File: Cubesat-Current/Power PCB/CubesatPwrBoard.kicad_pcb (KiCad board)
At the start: 2 copper layers, 90 x 96 mm, 57 parts, among them J1 SystemLoad, J10 Test_Point, J11 Test_Point, J14 Test_Point, J15 Test_Point, J16 Test_Point_GND, J2 SystemLoad, J3 I2C, J6 Test_Point, J7 Test_Point, Q1 TQM110NB04CR_RLG, Q2 2N7002*, U1 LTC4162

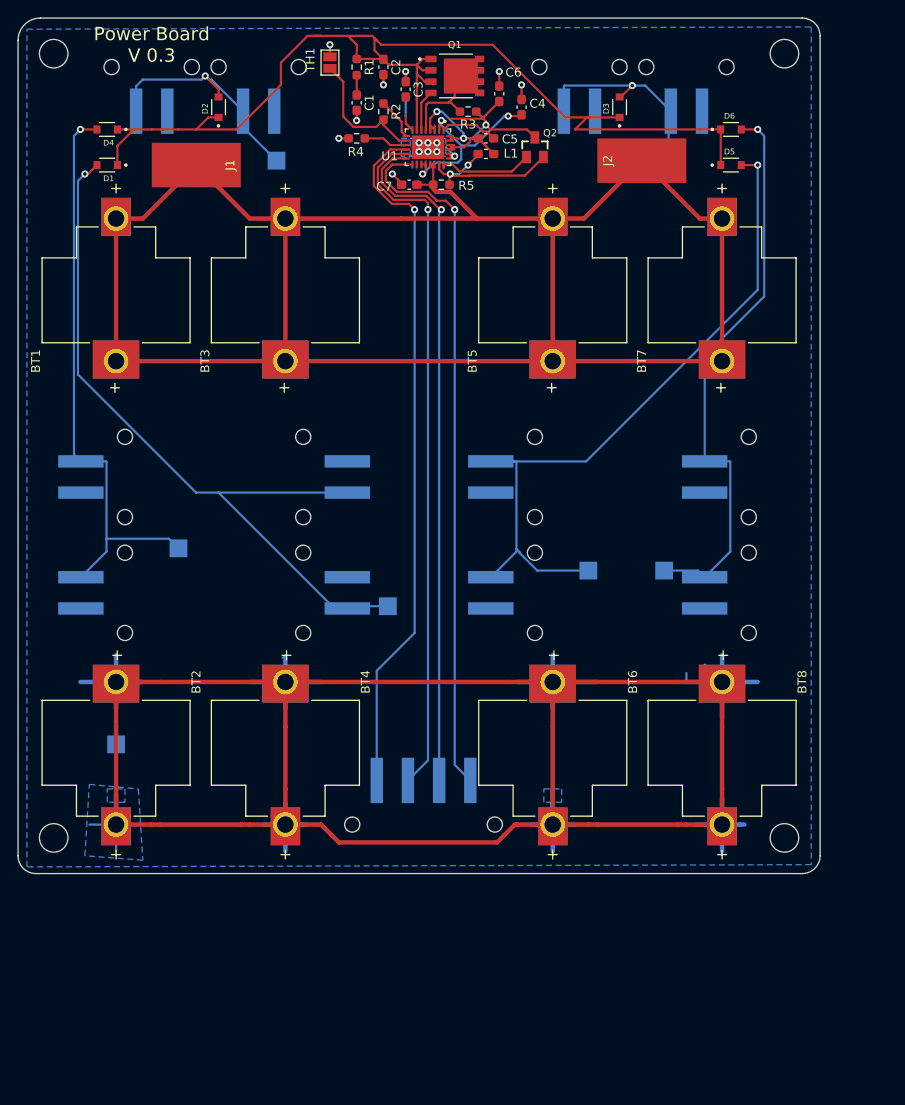
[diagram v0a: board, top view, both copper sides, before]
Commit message: Major revision to power board, three battery design v1
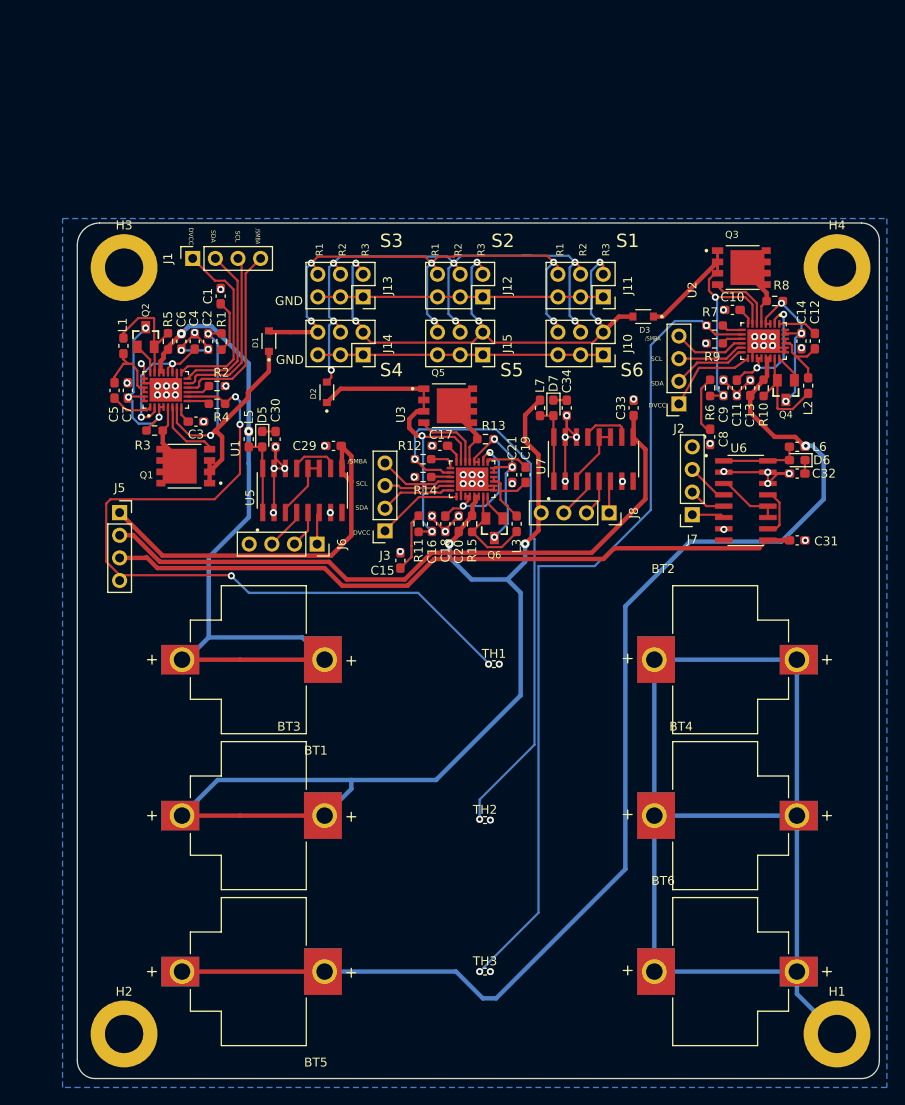
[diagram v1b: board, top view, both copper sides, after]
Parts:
- removed BT7, BT8: 254TR, 254TR:BAT_254TR
- removed D4: D_Schottky_Small, CUS520,H3F:DIO_CUS520,H3F
- removed J16: Test_Point_GND, TestPoint:TestPoint_Pad_2.0x2.0mm
- removed REF** (x4): MountingHole_3.2mm_M3, MountingHole:MountingHole_3.2mm_M3
- removed SC1, SC10, SC11, SC12, SC2, SC3, SC4, SC5, SC6, SC7, SC8, SC9: Solar_Cells, 6915_1x2:691508110302
- added C10: 1u, Capacitor_SMD:C_0603_1608Metric_Pad1.08x0.95mm_HandSolder, F.Cu at (180.2, 55.2)
- added C11: 4.7u, Capacitor_SMD:C_0603_1608Metric_Pad1.08x0.95mm_HandSolder, F.Cu at (180.7, 64.0)
- added C12: C, Capacitor_SMD:C_0603_1608Metric_Pad1.08x0.95mm_HandSolder, F.Cu at (189.4, 58.8)
- added C13: 10u, Capacitor_SMD:C_0603_1608Metric_Pad1.08x0.95mm_HandSolder, F.Cu at (182.2, 64.0)
- added C14: 10u, Capacitor_SMD:C_0603_1608Metric_Pad1.08x0.95mm_HandSolder, F.Cu at (187.9, 58.8)
- added C15: 150u, Capacitor_SMD:C_0603_1608Metric_Pad1.08x0.95mm_HandSolder, F.Cu at (142.9, 83.4)
- added C16: C_Polarized_US, Capacitor_SMD:C_0603_1608Metric_Pad1.08x0.95mm_HandSolder, F.Cu at (146.5, 79.2)
- added C17: 1u, Capacitor_SMD:C_0603_1608Metric_Pad1.08x0.95mm_HandSolder, F.Cu at (147.3, 70.5)
- added C18: 4.7u, Capacitor_SMD:C_0603_1608Metric_Pad1.08x0.95mm_HandSolder, F.Cu at (148.0, 79.2)
- added C19: C, Capacitor_SMD:C_0603_1608Metric_Pad1.08x0.95mm_HandSolder, F.Cu at (157.0, 73.8)
- added C20: 10u, Capacitor_SMD:C_0603_1608Metric_Pad1.08x0.95mm_HandSolder, F.Cu at (149.5, 79.2)
- added C21: 10u, Capacitor_SMD:C_0603_1608Metric_Pad1.08x0.95mm_HandSolder, F.Cu at (155.5, 73.8)
- added C29: C_Polarized_US, Capacitor_SMD:C_0603_1608Metric_Pad1.08x0.95mm_HandSolder, F.Cu at (135.4, 70.5)
- added C30: C_Polarized_US, Capacitor_SMD:C_0603_1608Metric_Pad1.08x0.95mm_HandSolder, F.Cu at (128.9, 69.8)
- added C31: 4.7u, Capacitor_SMD:C_0603_1608Metric_Pad1.08x0.95mm_HandSolder, F.Cu at (187.4, 81.1)
- added C32: 100u, Capacitor_SMD:C_0603_1608Metric_Pad1.08x0.95mm_HandSolder, F.Cu at (187.4, 73.6)
- added C33: 4.7u, Capacitor_SMD:C_0603_1608Metric_Pad1.08x0.95mm_HandSolder, F.Cu at (169.1, 66.2)
- added C34: 100u, Capacitor_SMD:C_0603_1608Metric_Pad1.08x0.95mm_HandSolder, F.Cu at (161.6, 66.2)
- added C8: 150u, Capacitor_SMD:C_0603_1608Metric_Pad1.08x0.95mm_HandSolder, F.Cu at (177.7, 69.5)
- added C9: C_Polarized_US, Capacitor_SMD:C_0603_1608Metric_Pad1.08x0.95mm_HandSolder, F.Cu at (179.2, 64.0)
- added D7: D_Schottky, Diode_SMD:D_0603_1608Metric_Pad1.05x0.95mm_HandSolder, F.Cu at (160.1, 66.2)
- added H1: MountingHole_Pad, MountingHole:MountingHole_4.3mm_M4_DIN965_Pad, F.Cu at (191.9, 136.5)
- added H2: MountingHole_Pad, MountingHole:MountingHole_4.3mm_M4_DIN965_Pad, F.Cu at (111.9, 136.5)
- added H3: MountingHole_Pad, MountingHole:MountingHole_4.3mm_M4_DIN965_Pad, F.Cu at (111.9, 50.5)
- added H4: MountingHole_Pad, MountingHole:MountingHole_4.3mm_M4_DIN965_Pad, F.Cu at (191.9, 50.5)
- added J12: S3, Connector_PinSocket_2.54mm:PinSocket_2x03_P2.54mm_Vertical, F.Cu at (152.2, 53.8)
- added J13: S4, Connector_PinSocket_2.54mm:PinSocket_2x03_P2.54mm_Vertical, F.Cu at (138.7, 53.8)
- added J5: Conn_01x04_Female, Connector_PinSocket_2.54mm:PinSocket_1x04_P2.54mm_Vertical, F.Cu at (111.4, 78.0)
- added J8: Conn_01x03_Female, Connector_PinSocket_2.54mm:PinSocket_1x04_P2.54mm_Vertical, F.Cu at (166.3, 78.0)
- added L2: 4.7u, Inductor_SMD:L_0603_1608Metric_Pad1.05x0.95mm_HandSolder, F.Cu at (188.7, 63.8)
- added L3: 4.7u, Inductor_SMD:L_0603_1608Metric_Pad1.05x0.95mm_HandSolder, F.Cu at (156.0, 79.2)
- added L5: L, Inductor_SMD:L_0603_1608Metric_Pad1.05x0.95mm_HandSolder, F.Cu at (125.9, 69.8)
- added L6: 22u, Inductor_SMD:L_0603_1608Metric_Pad1.05x0.95mm_HandSolder, F.Cu at (187.4, 70.6)
- added L7: 22u, Inductor_SMD:L_0603_1608Metric_Pad1.05x0.95mm_HandSolder, F.Cu at (158.6, 66.2)
- added Q3: TQM110NB04CR_RLG, TQM110N:TRANS_TQM110NB04CR_RLG, F.Cu at (181.2, 50.5)
- added Q4: 2N7002*, 2N7002:SOT23, F.Cu at (186.2, 64.2)
- added Q5: TQM110NB04CR_RLG, TQM110N:TRANS_TQM110NB04CR_RLG, F.Cu at (148.2, 66.0)
- added Q6: 2N7002*, 2N7002:SOT23, F.Cu at (153.5, 79.8)
- added R10: 10m, Resistor_SMD:R_0603_1608Metric_Pad0.98x0.95mm_HandSolder, F.Cu at (183.7, 64.0)
- added R11: 2.5, Resistor_SMD:R_0603_1608Metric_Pad0.98x0.95mm_HandSolder, F.Cu at (145.0, 79.2)
- added R12: 16m, Resistor_SMD:R_0603_1608Metric_Pad0.98x0.95mm_HandSolder, F.Cu at (145.5, 72.0)
- added R13: 16m, Resistor_SMD:R_0603_1608Metric_Pad0.98x0.95mm_HandSolder, F.Cu at (152.5, 69.8)
- added R14: 63.4k, Resistor_SMD:R_0603_1608Metric_Pad0.98x0.95mm_HandSolder, F.Cu at (145.5, 74.0)
- added R15: 10m, Resistor_SMD:R_0603_1608Metric_Pad0.98x0.95mm_HandSolder, F.Cu at (151.0, 79.2)
- added R6: 2.5, Resistor_SMD:R_0603_1608Metric_Pad0.98x0.95mm_HandSolder, F.Cu at (177.7, 64.0)
- added R7: 16m, Resistor_SMD:R_0603_1608Metric_Pad0.98x0.95mm_HandSolder, F.Cu at (178.2, 57.0)
- added R8: 16m, Resistor_SMD:R_0603_1608Metric_Pad0.98x0.95mm_HandSolder, F.Cu at (184.9, 54.2)
- added R9: 63.4k, Resistor_SMD:R_0603_1608Metric_Pad0.98x0.95mm_HandSolder, F.Cu at (178.2, 59.0)
- added TH2: Thermistor_NTC, Resistor_SMD:R_0402_1005Metric_Pad0.72x0.64mm_HandSolder, F.Cu at (152.4, 112.5)
- added TH3: Thermistor_NTC, Resistor_SMD:R_0402_1005Metric_Pad0.72x0.64mm_HandSolder, F.Cu at (152.4, 129.5)
- added U2: LTC4162, LTC4162:QFN50P500X400X80-29N, F.Cu at (183.7, 58.8)
- added U3: LTC4162, LTC4162:QFN50P500X400X80-29N, F.Cu at (151.0, 74.2)
- added U5: MAX710ESE+T, MAX710ESE:SOIC127P600X175-16N, F.Cu at (131.9, 75.5)
- added U6: MAX710ESE+T, MAX710ESE:SOIC127P600X175-16N, F.Cu at (181.7, 76.6)
- added U7: MAX710ESE+T, MAX710ESE:SOIC127P600X175-16N, F.Cu at (164.6, 72.0)
- C1: value 150u -> C_Polarized_US
- C2: value 0.1u -> C_Polarized_US
- C3: value 1u -> C
- C4: value 4.7u -> C
- C5: value 22n -> C
- C6, C7: value 10u -> C
- D5, D6: value D_Schottky_Small -> D_Schottky; footprint CUS520,H3F:DIO_CUS520,H3F -> Diode_SMD:D_0603_1608Metric_Pad1.05x0.95mm_HandSolder
- J1, J2: value SystemLoad -> Conn_01x04_Female; footprint Connector_Wire:SolderWirePad_1x01_SMD_5x10mm -> Connector_PinSocket_2.54mm:PinSocket_1x04_P2.54mm_Vertical
- J10: value Test_Point -> S1; footprint TestPoint:TestPoint_Pad_2.0x2.0mm -> Connector_PinSocket_2.54mm:PinSocket_2x03_P2.54mm_Vertical; moved to F.Cu
- J11: value Test_Point -> S2; footprint TestPoint:TestPoint_Pad_2.0x2.0mm -> Connector_PinSocket_2.54mm:PinSocket_2x03_P2.54mm_Vertical; moved to F.Cu
- J14: value Test_Point -> S5; footprint TestPoint:TestPoint_Pad_2.0x2.0mm -> Connector_PinSocket_2.54mm:PinSocket_2x03_P2.54mm_Vertical; moved to F.Cu
- J15: value Test_Point -> S6; footprint TestPoint:TestPoint_Pad_2.0x2.0mm -> Connector_PinSocket_2.54mm:PinSocket_2x03_P2.54mm_Vertical; moved to F.Cu
- J3: value I2C -> Conn_01x04_Female; footprint 6915_1x4:691508110304 -> Connector_PinSocket_2.54mm:PinSocket_1x04_P2.54mm_Vertical; moved to F.Cu
- J6, J7: value Test_Point -> Conn_01x03_Female; footprint TestPoint:TestPoint_Pad_2.0x2.0mm -> Connector_PinSocket_2.54mm:PinSocket_1x04_P2.54mm_Vertical; moved to F.Cu
- L1: value 4.7u -> L
- R1: value 2.5 -> R
- R2, R3: value 16m -> R
- R4: value 63.4k -> R
- R5: value 10m -> R
- TH1: footprint Jumper:SolderJumper-2_P1.3mm_Open_Pad1.0x1.5mm -> Resistor_SMD:R_0402_1005Metric_Pad0.72x0.64mm_HandSolder
- moved BT5 83.6 mm to (126.4, 129.5), turned to 180 degrees
- moved TH1 70.0 mm to (153.4, 95.0), turned to 0 degrees
- moved BT2 69.2 mm to (179.4, 94.5), turned to 0 degrees
- moved J7 61.3 mm to (175.7, 78.2), turned to 180 degrees
- moved D5 60.9 mm to (127.4, 69.8), turned to -90 degrees
- moved BT3 59.1 mm to (126.4, 112.0), turned to 180 degrees
- moved J11 55.4 mm to (165.7, 53.8), turned to -90 degrees
- moved Q1 53.2 mm to (118.8, 72.8), turned to 180 degrees
- moved C5 50.4 mm to (110.8, 64.3), turned to 90 degrees
- moved R3 50.2 mm to (115.3, 68.8), turned to 0 degrees
- moved BT4 49.9 mm to (179.4, 112.0), turned to 0 degrees
- moved Q2 48.6 mm to (114.3, 58.3)
- moved L1 46.0 mm to (111.8, 59.3), turned to 90 degrees
- moved C6 45.2 mm to (118.3, 58.8), turned to -90 degrees
- moved C4 45.1 mm to (119.8, 58.8)
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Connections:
- net Net-(R2-Pad2) renamed /Bat_Reg_1/TH
- BT1 pad P1_1: Net-(BT1-PadP1_1) -> /Bat_Reg_1/V_Bat
- BT1 pad P1_2: Net-(BT1-PadP1_1) -> /Bat_Reg_1/V_Bat
- BT3 pad P1_1: Net-(BT1-PadP1_1) -> /Bat_Reg_2/V_Bat
- BT3 pad P1_2: Net-(BT1-PadP1_1) -> /Bat_Reg_2/V_Bat
- BT5 pad P1_1: Net-(BT1-PadP1_1) -> /Bat_Reg_3/V_Bat
- BT5 pad P1_2: Net-(BT1-PadP1_1) -> /Bat_Reg_3/V_Bat
- C2 pad 1: Net-(C2-Pad1) -> /Bat_Reg_1/VIN
- C6 pad 1: Net-(C6-Pad1) -> /Bat_Reg_1/V_Bat
- C7 pad 1: Net-(BT1-PadP1_1) -> Net-(C7-Pad1)
- D1 pad 1: Net-(C2-Pad1) -> /Bat_Reg_1/VIN
- D2 pad 1: Net-(C2-Pad1) -> /Bat_Reg_2/VIN
- D3 pad 1: Net-(C2-Pad1) -> /Bat_Reg_3/VIN
- D5 pad 1: Net-(C2-Pad1) -> Net-(C30-Pad1)
- D6 pad 1: Net-(C2-Pad1) -> Net-(C32-Pad1)
- J1 pad 1: Net-(BT1-PadP1_1) -> /Bat_Reg_1/DVCC
- J10 pad 1: Net-(D3-Pad2) -> GND
- J11 pad 1: Net-(D4-Pad2) -> GND
- J14 pad 1: Net-(D5-Pad2) -> GND
- J15 pad 1: Net-(D6-Pad2) -> GND
- J2 pad 1: Net-(BT1-PadP1_1) -> /Bat_Reg_3/DVCC
- J3 pad 1: Net-(J3-Pad1) -> /Bat_Reg_2/DVCC
- J3 pad 2: Net-(J3-Pad2) -> /Bat_Reg_2/SDA
- J3 pad 3: Net-(J3-Pad3) -> /Bat_Reg_2/SCL
- J3 pad 4: Net-(J3-Pad4) -> /Bat_Reg_2//SMBALERT
- J6 pad 1: Net-(D1-Pad2) -> /V_Reg_3.3_5V1/3/#5
- J7 pad 1: Net-(D2-Pad2) -> /V_Reg_3.3_5V3/3/#5
- Q1 pad 1: Net-(C2-Pad1) -> /Bat_Reg_1/VIN
- Q1 pad 2: Net-(C2-Pad1) -> /Bat_Reg_1/VIN
- Q1 pad 3: Net-(C2-Pad1) -> /Bat_Reg_1/VIN
- Q2 pad 3: Net-(C6-Pad1) -> Net-(C7-Pad1)
- R1 pad 1: Net-(C2-Pad1) -> /Bat_Reg_1/VIN
- R3 pad 1: Net-(C6-Pad1) -> Net-(C7-Pad1)
- R5 pad 1: Net-(BT1-PadP1_1) -> /Bat_Reg_1/V_Bat
- U1 pad 12: Net-(J3-Pad4) -> /Bat_Reg_1//SMBALERT
- U1 pad 13: Net-(J3-Pad3) -> /Bat_Reg_1/SCL
- U1 pad 14: Net-(J3-Pad2) -> /Bat_Reg_1/SDA
- U1 pad 15: Net-(J3-Pad1) -> /Bat_Reg_1/DVCC
- U1 pad 19: Net-(BT1-PadP1_1) -> /Bat_Reg_1/V_Bat
- U1 pad 20: Net-(BT1-PadP1_1) -> /Bat_Reg_1/V_Bat
- U1 pad 27: Net-(C6-Pad1) -> Net-(C7-Pad1)
- U1 pad 28: Net-(C6-Pad1) -> Net-(C7-Pad1)
- U1 pad 3: Net-(C6-Pad1) -> Net-(C7-Pad1)
- U1 pad 4: Net-(C6-Pad1) -> Net-(C7-Pad1)
- U1 pad 7: Net-(C2-Pad1) -> /Bat_Reg_1/VIN
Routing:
- net Net-(BT1-PadP1_1): track 221.8 -> 0.00 mm
- net /Bat_Reg_3/V_Bat: track 0.00 -> 136.4 mm, vias 0 -> 1
- net Net-(C2-Pad1): track 123.7 -> 0.00 mm
- net /Bat_Reg_2/V_Bat: track 0.00 -> 117.6 mm, vias 0 -> 2
- net /Bat_Reg_3/TH: track 0.00 -> 93.9 mm, vias 0 -> 2
- net /Bat_Reg_1/V_Bat: track 0.00 -> 81.9 mm, vias 0 -> 2
- net /V_Reg_3.3_5V3/Vout: track 0.00 -> 78.7 mm
- net Net-(J3-Pad1): track 78.2 -> 0.00 mm, vias 1 -> 0
- net Net-(J3-Pad4): track 78.1 -> 0.00 mm, vias 1 -> 0
- net Net-(J3-Pad3): track 77.9 -> 0.00 mm, vias 1 -> 0
- net Net-(J3-Pad2): track 76.8 -> 0.00 mm, vias 1 -> 0
- net /V_Reg_3.3_5V2/Vout: track 0.00 -> 74.8 mm
- net Net-(D5-Pad2): track 79.9 -> 8.89 mm, vias 1 -> 0
- net /Bat_Reg_1/TH: track 15.6 -> 85.6 mm, vias 0 -> 4
- net Net-(D4-Pad2): track 65.3 -> 0.00 mm, vias 1 -> 0
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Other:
- net class Battery removed
- net class Default removed
- board text added: "/SMBA"
- board text added: "DVCC"
- board text added: "GND"
- board text added: "R1 R2 R3"
- board text added: "S1"
- board text added: "S2"
- board text added: "S3"
- board text added: "S4"
- board text added: "S5"
- board text added: "S6"
- board text added: "SCL"
- board text added: "SDA"
- board text removed: "I2C"
- board text removed: "Power Board V 0.3"
- board text removed: "SIDE 1"
- board text removed: "SIDE 2"
- board text removed: "SIDE 3"
- board text removed: "SIDE 4"
- board text removed: "SIDE 5"
- board text removed: "SIDE 6"

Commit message: added to silkscreen and exported fabrication files
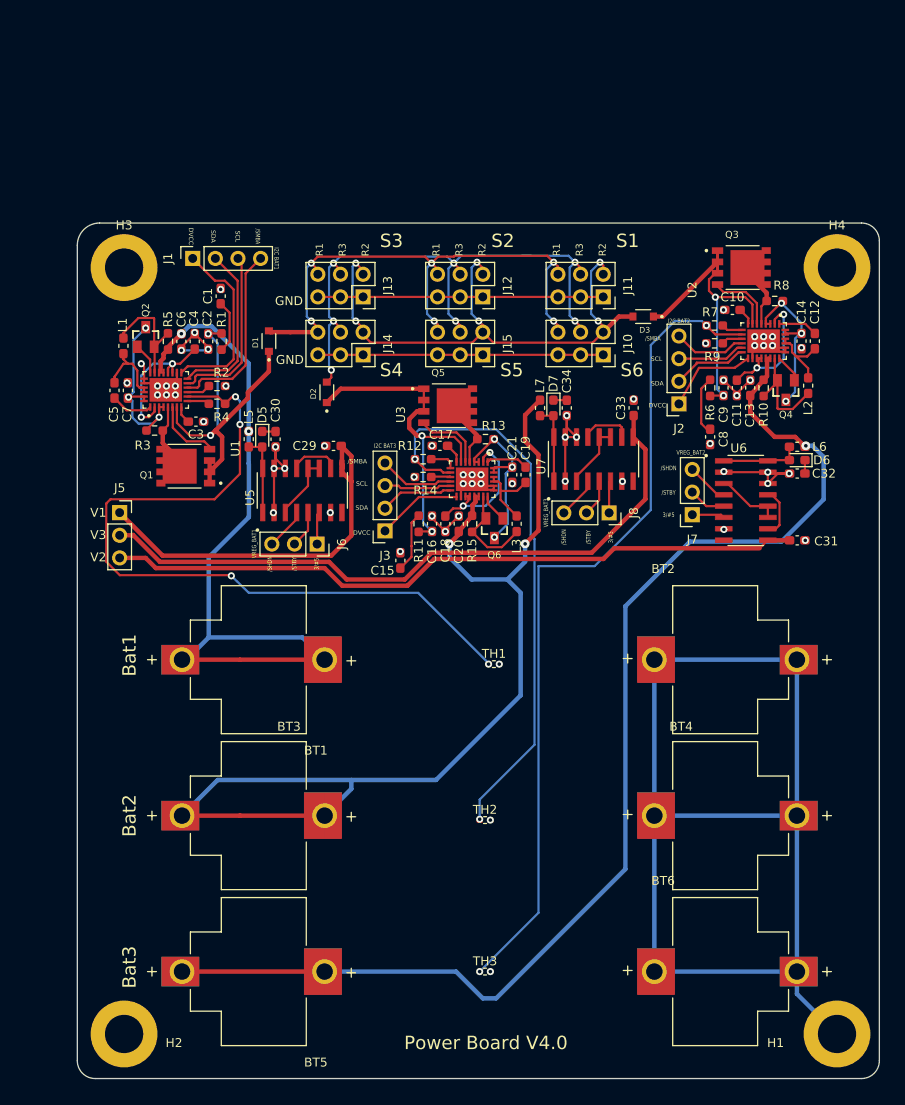
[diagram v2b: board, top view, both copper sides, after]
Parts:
- J5, J6, J7, J8: footprint Connector_PinSocket_2.54mm:PinSocket_1x04_P2.54mm_Vertical -> Connector_PinSocket_2.54mm:PinSocket_1x03_P2.54mm_Vertical
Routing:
- removed copper zone on B.Cu, net GND
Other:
- board text added: "/SHDN"
- board text added: "/STBY"
- board text added: "3/#5"
- board text added: "Bat1"
- board text added: "Bat2"
- board text added: "Bat3"
- board text added: "I2C BAT1"
- board text added: "I2C BAT2"
- board text added: "I2C BAT3"
- board text added: "Power Board V4.0"
- board text added: "R1 R3 R2"
- board text added: "V1"
- board text added: "V2"
- board text added: "V3"
- board text added: "VREG_BAT1"
- board text added: "VREG_BAT2"
- board text added: "VREG_BAT3"
- board text removed: "R1 R2 R3"

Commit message: Forgot to readd ground plane after making changes
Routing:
- added copper zone on B.Cu, net GND
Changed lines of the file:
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@@
   (segment (start 113.5 56.1625) (end 115.2 56.1625) (width 0.25) (layer "F.Cu") (net 88))
   (segment (start 111.825 57.8375) (end 113.5 56.1625) (width 0.25) (layer "F.Cu") (net 88))
+  (zone (net 2) (net_name "GND") (layer "B.Cu") (hatch edge 0.508)
+    (connect_pads (clearance 0.508))
+    (min_thickness 0.254) (filled_areas_thickness no)
+    (fill yes (thermal_gap 0.508) (thermal_bridge_width 0.508) (island_removal_mode 2) (island_area_min 0))
+    (polygon
+      (pts
+        (xy 197 142)
+        (xy 106 142)
+        (xy 106 45)
+        (xy 197 45)
+      )
+    )
+  )
   (group "" (id 062e1a51-5270-4df1-a09d-e80b2cec1905)
     (members

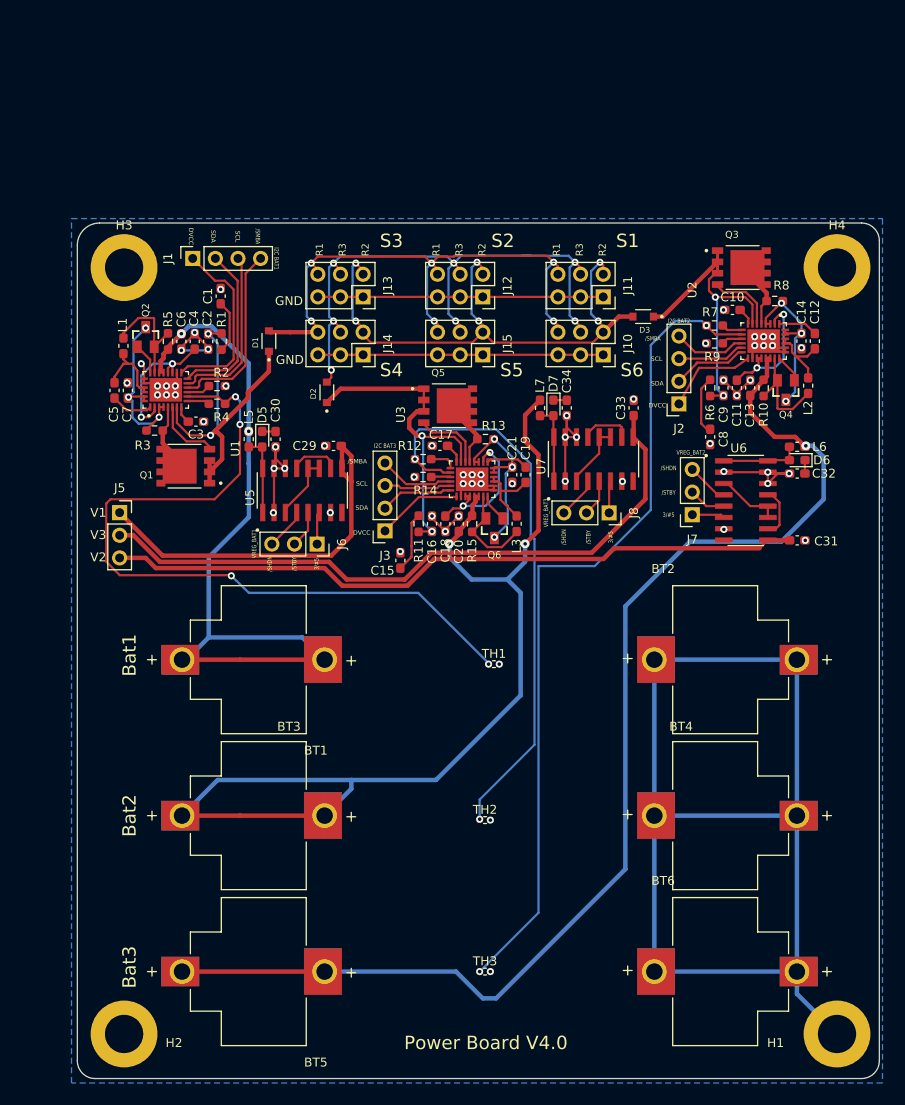
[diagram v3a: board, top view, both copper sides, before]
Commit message: Fixed footprint size of 150uF caps
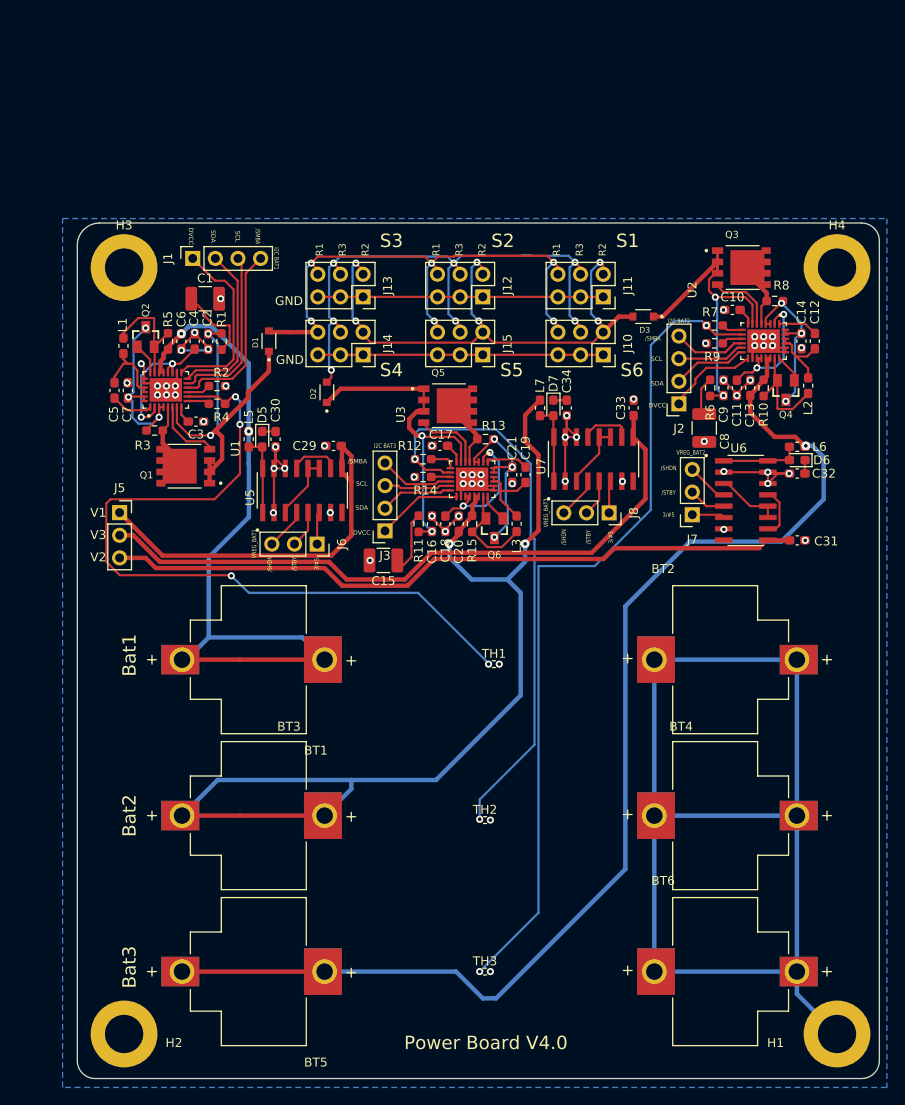
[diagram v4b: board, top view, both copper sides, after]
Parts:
- C1, C15, C8: footprint Capacitor_SMD:C_0603_1608Metric_Pad1.08x0.95mm_HandSolder -> Capacitor_SMD:C_1210_3225Metric_Pad1.33x2.70mm_HandSolder
- moved C15 1.90 mm to (141.0, 83.4), turned to 180 degrees
- moved C1 1.76 mm to (121.0, 54.0), turned to 0 degrees
- moved C8 1.20 mm to (177.0, 68.5)
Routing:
- net Net-(C1-Pad1): track 5.94 -> 8.88 mm
- net Net-(C8-Pad1): track 6.59 -> 4.40 mm
